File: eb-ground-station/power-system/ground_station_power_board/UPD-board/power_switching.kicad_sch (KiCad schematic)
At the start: 22 parts

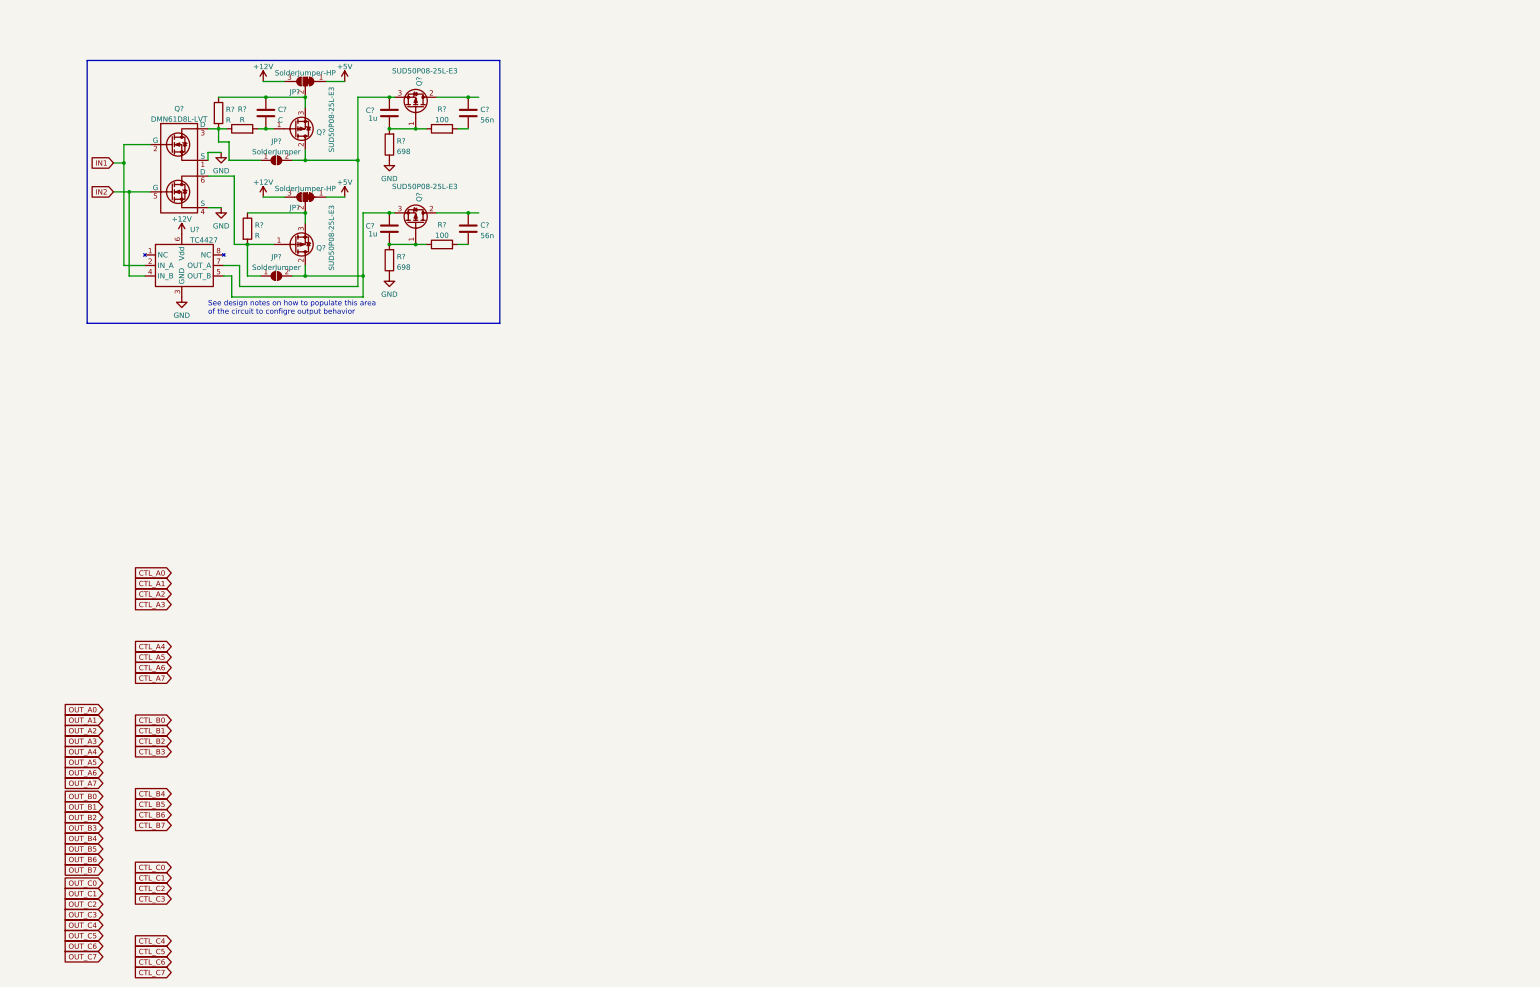
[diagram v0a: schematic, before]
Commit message: New power board schematic almost done
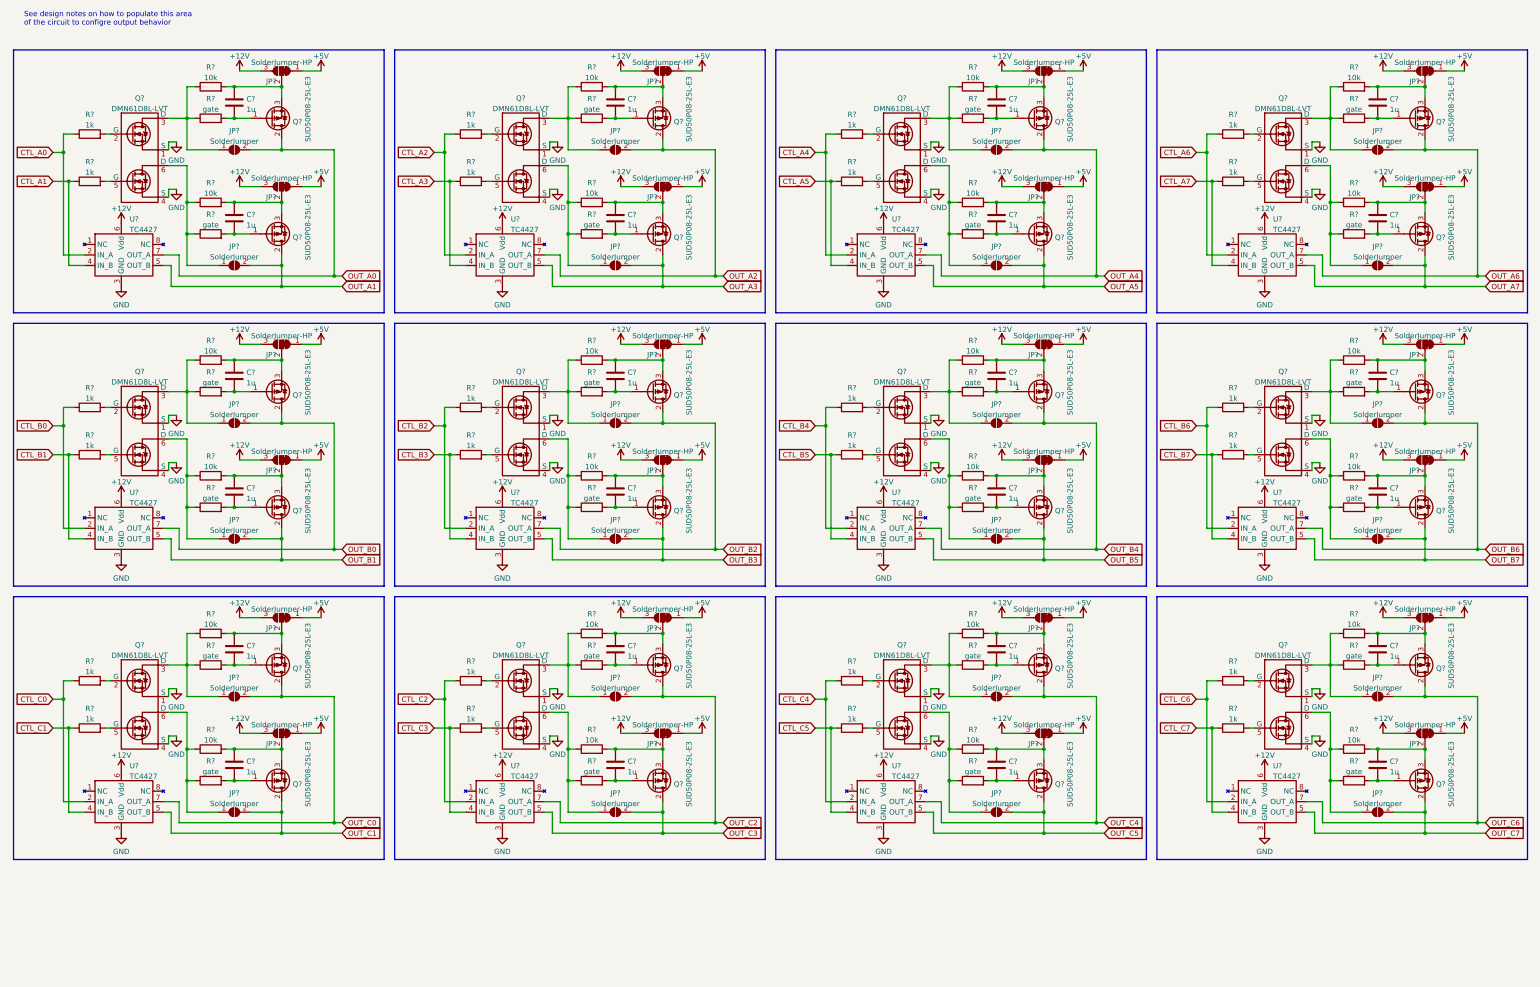
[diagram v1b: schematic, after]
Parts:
- removed C? (x2): 1u, symbol Device:C
- removed C? (x2): 56n, symbol Device:C
- removed Q? (x2): SUD50P08-25L-E3, symbol Device:Q_PMOS_GDS
- removed R? (x2): 698, symbol Device:R
- removed R? (x2): 100, symbol Device:R
- added C? (x23): 1u, symbol Device:C
- added JP? (x22): SolderJumper, symbol Jumper:SolderJumper_2_Open
- added JP? (x22): SolderJumper-HP, symbol Jumper:SolderJumper_3_Bridged12
- added Q? (x11): DMN61D8L-LVT, symbol OreSat-q-mosfet-DMN61D8L-LVT:DMN61D8L-LVT
- added Q? (x22): SUD50P08-25L-E3, symbol Device:Q_PMOS_GDS
- added R? (x24): 1k, symbol Device:R
- added R? (x23): gate, symbol Device:R
- added R? (x22): 10k, symbol Device:R
- added U? (x11): TC4427, symbol OreSat-q-mosfet-driver-TC4427:TC4427
- C?: value C -> 1u
- R? (x2): value R -> 10k
- R?: value R -> gate
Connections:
- net +12V: now also JP?.3 (B), JP?.3 (B), JP?.3 (B), JP?.3 (B), JP?.3 (B), JP?.3 (B), JP?.3 (B), JP?.3 (B), JP?.3 (B), JP?.3 (B), JP?.3 (B), JP?.3 (B), JP?.3 (B), JP?.3 (B), JP?.3 (B), JP?.3 (B), JP?.3 (B), JP?.3 (B), JP?.3 (B), JP?.3 (B), JP?.3 (B), JP?.3 (B), U?.6 (Vdd), U?.6 (Vdd), U?.6 (Vdd), U?.6 (Vdd), U?.6 (Vdd), U?.6 (Vdd), U?.6 (Vdd), U?.6 (Vdd), U?.6 (Vdd), U?.6 (Vdd), U?.6 (Vdd)
- net +5V: now also JP?.1 (A), JP?.1 (A), JP?.1 (A), JP?.1 (A), JP?.1 (A), JP?.1 (A), JP?.1 (A), JP?.1 (A), JP?.1 (A), JP?.1 (A), JP?.1 (A), JP?.1 (A), JP?.1 (A), JP?.1 (A), JP?.1 (A), JP?.1 (A), JP?.1 (A), JP?.1 (A), JP?.1 (A), JP?.1 (A), JP?.1 (A), JP?.1 (A)
- net CTL_A0: now also U?.2 (IN_A), R?.1
- net CTL_A1: now also U?.4 (IN_B), R?.1
- net CTL_A2: now also R?.1, U?.2 (IN_A)
- net CTL_A3: now also R?.1, U?.4 (IN_B)
- net CTL_A4: now also R?.1, U?.2 (IN_A)
- net CTL_A5: now also R?.1, U?.4 (IN_B)
- net CTL_A6: now also R?.1, U?.2 (IN_A)
- net CTL_A7: now also R?.1, U?.4 (IN_B)
- net CTL_B0: now also R?.1, U?.2 (IN_A)
- net CTL_B1: now also R?.1, U?.4 (IN_B)
- net CTL_B2: now also R?.1, U?.2 (IN_A)
- net CTL_B3: now also R?.1, U?.4 (IN_B)
- net CTL_B4: now also R?.1, U?.2 (IN_A)
- net CTL_B5: now also R?.1, U?.4 (IN_B)
- net CTL_B6: now also R?.1, U?.2 (IN_A)
- net CTL_B7: now also R?.1, U?.4 (IN_B)
- net CTL_C0: now also R?.1, U?.2 (IN_A)
- net CTL_C1: now also R?.1, U?.4 (IN_B)
- net CTL_C2: now also R?.1, U?.2 (IN_A)
- net CTL_C3: now also R?.1, U?.4 (IN_B)
- net CTL_C4: now also R?.1, U?.2 (IN_A)
- net CTL_C5: now also R?.1, U?.4 (IN_B)
- net CTL_C6: now also R?.1, U?.2 (IN_A)
- net CTL_C7: now also R?.1, U?.4 (IN_B)
- net GND: now also Q?.1 (S), Q?.1 (S), Q?.1 (S), Q?.1 (S), Q?.1 (S), Q?.1 (S), Q?.1 (S), Q?.1 (S), Q?.1 (S), Q?.1 (S), Q?.1 (S), Q?.4 (S), Q?.4 (S), Q?.4 (S), Q?.4 (S), Q?.4 (S), Q?.4 (S), Q?.4 (S), Q?.4 (S), Q?.4 (S), Q?.4 (S), Q?.4 (S), U?.3 (GND), U?.3 (GND), U?.3 (GND), U?.3 (GND), U?.3 (GND), U?.3 (GND), U?.3 (GND), U?.3 (GND), U?.3 (GND), U?.3 (GND), U?.3 (GND)
- net OUT_A0: now also JP?.2 (B), Q?.2 (D), U?.7 (OUT_A)
- net OUT_A1: now also JP?.2 (B), Q?.2 (D), U?.5 (OUT_B)
- net OUT_A2: now also JP?.2 (B), Q?.2 (D), U?.7 (OUT_A)
- net OUT_A3: now also JP?.2 (B), Q?.2 (D), U?.5 (OUT_B)
- net OUT_A4: now also JP?.2 (B), Q?.2 (D), U?.7 (OUT_A)
- net OUT_A5: now also JP?.2 (B), Q?.2 (D), U?.5 (OUT_B)
- net OUT_A6: now also JP?.2 (B), Q?.2 (D), U?.7 (OUT_A)
- net OUT_A7: now also JP?.2 (B), Q?.2 (D), U?.5 (OUT_B)
- net OUT_B0: now also JP?.2 (B), Q?.2 (D), U?.7 (OUT_A)
- net OUT_B1: now also JP?.2 (B), Q?.2 (D), U?.5 (OUT_B)
- net OUT_B2: now also JP?.2 (B), Q?.2 (D), U?.7 (OUT_A)
- net OUT_B3: now also JP?.2 (B), Q?.2 (D), U?.5 (OUT_B)
- net OUT_B4: now also JP?.2 (B), Q?.2 (D), U?.7 (OUT_A)
- net OUT_B5: now also JP?.2 (B), Q?.2 (D), U?.5 (OUT_B)
- net OUT_B6: now also JP?.2 (B), Q?.2 (D), U?.7 (OUT_A)
- net OUT_B7: now also JP?.2 (B), Q?.2 (D), U?.5 (OUT_B)
- net OUT_C0: now also JP?.2 (B), Q?.2 (D), U?.7 (OUT_A)
- net OUT_C1: now also JP?.2 (B), Q?.2 (D), U?.5 (OUT_B)
- net OUT_C2: now also JP?.2 (B), Q?.2 (D), U?.7 (OUT_A)
- net OUT_C3: now also JP?.2 (B), Q?.2 (D), U?.5 (OUT_B)
- net OUT_C4: now also JP?.2 (B), Q?.2 (D), U?.7 (OUT_A)
- net OUT_C5: now also JP?.2 (B), Q?.2 (D), U?.5 (OUT_B)
- net OUT_C6: now also JP?.2 (B), Q?.2 (D), U?.7 (OUT_A)
- net OUT_C7: now also JP?.2 (B), Q?.2 (D), U?.5 (OUT_B)
- net at C?.1, JP?.2 (C), Q?.3 (S): now also R?.2; no longer R?.1
- net at JP?.1 (A), Q?.3 (D), R?.1: now also R?.1; no longer R?.2
- net at JP?.2 (C), Q?.3 (S): now also R?.2, C?.1; no longer R?.1
- net at JP?.1 (A), Q?.6 (D): now also R?.1, R?.1; no longer Q?.1 (G), R?.2
- net IN1: no longer names the net of Q?.2 (G)
- net IN1: now also R?.2; no longer U?.2 (IN_A)
- net IN2: no longer names the net of Q?.5 (G)
- net IN2: now also R?.2; no longer U?.4 (IN_B)
- new net: Q?.2 (G), R?.2 (x11)
- new net: JP?.1 (A), Q?.3 (D), R?.1, R?.1 (x11)
- new net: Q?.5 (G), R?.2 (x11)
- new net: JP?.1 (A), Q?.6 (D), R?.1, R?.1 (x11)
- new net: C?.2, Q?.1 (G), R?.2 (x23)
- new net: C?.1, JP?.2 (C), Q?.3 (S), R?.2 (x22)
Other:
- moved on the sheet: C?, JP?, Q?, R?, U?

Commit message: First layout done. No slikscreen work yet
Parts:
- removed C? (x16): 1u, symbol Device:C
- removed JP? (x16): SolderJumper, symbol Jumper:SolderJumper_2_Open
- removed JP? (x20): SolderJumper-HP, symbol Jumper:SolderJumper_3_Bridged12
- removed Q? (x7): DMN61D8L-LVT, symbol OreSat-q-mosfet-DMN61D8L-LVT:DMN61D8L-LVT
- removed Q? (x16): SUD50P08-25L-E3, symbol Device:Q_PMOS_GDS
- removed R? (x24): 1k, symbol Device:R
- removed R? (x16): gate, symbol Device:R
- removed R? (x16): 10k, symbol Device:R
- removed U? (x7): TC4427, symbol OreSat-q-mosfet-driver-TC4427:TC4427
- added Q10, Q13, Q14, Q2, Q6, Q7, Q9: DMN61D8L-LVT, oresat-footprints:TSOT26-6, symbol OreSat-q-mosfet-DMN61D8L-LVT:DMN61D8L-LVT
- added RN13, RN14, RN15, RN16, RN17, RN18: 10k, Resistor_SMD:R_Array_Convex_4x0603, symbol Device:R_Pack04
- added U10, U11, U12, U14, U15, U16, U17: TC4427, Package_SO:MSOP-8_3x3mm_P0.65mm, symbol OreSat-q-mosfet-driver-TC4427:TC4427
- C12, C13, C14, C15, C16, C17, C18, C19: renamed from C?; footprint (none) -> Capacitor_SMD:C_0603_1608Metric; DPN (none) -> 1276-1184-2-ND; MPN (none) -> CL10B105KA8NNNC; Mfr (none) -> Samsung Electro-Mechanics
- JP14, JP15, JP18, JP19, JP22, JP23, JP26, JP27: renamed from JP?; footprint (none) -> oresat-footprints:SolderJumper-2_P1.3mm_Open_RoundedPad1.0x1.5mm
- JP24, JP25, JP28, JP29: renamed from JP?; footprint (none) -> oresat-footprints:JP-SOLDER-2way-HP
- Q1, Q15, Q18, Q3, Q8: renamed from Q?; footprint (none) -> oresat-footprints:TSOT26-6
- Q11, Q12, Q16, Q17, Q19, Q20, Q4, Q5: renamed from Q?; footprint (none) -> oresat-footprints:TO-252-3_TabIsPin2
- R10, R11, R12, R13, R14, R15, R16, R17, R18, R19, R20, R21, R22, R23, R8, R9: renamed from R?; footprint (none) -> Resistor_SMD:R_0603_1608Metric
- U13, U18, U19, U8, U9: renamed from U?; footprint (none) -> Package_SO:MSOP-8_3x3mm_P0.65mm
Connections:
- net +12V: now also C14.1, C15.1, Q11.3 (S), Q12.3 (S), R12.2, R14.2, U10.6 (Vdd), U11.6 (Vdd), U12.6 (Vdd), U14.6 (Vdd), U15.6 (Vdd), U16.6 (Vdd), U17.6 (Vdd)
- net +5V: now also C12.1, C13.1, Q4.3 (S), Q5.3 (S), R10.2, R8.2
- net CTL_A0: now also RN13.5 (R4.2)
- net CTL_A1: now also RN13.6 (R3.2)
- net CTL_A2: now also RN13.7 (R2.2)
- net CTL_A3: now also RN13.8 (R1.2)
- net CTL_A4: now also RN14.4 (R4.1)
- net CTL_A5: now also RN14.3 (R3.1)
- net CTL_A6: now also RN14.2 (R2.1)
- net CTL_A7: now also RN14.1 (R1.1)
- net CTL_B0: now also RN15.4 (R4.1)
- net CTL_B1: now also RN15.3 (R3.1)
- net CTL_B2: now also RN15.2 (R2.1), U11.2 (IN_A)
- net CTL_B3: now also RN15.1 (R1.1), U11.4 (IN_B)
- net CTL_B4: now also RN16.4 (R4.1), U14.2 (IN_A)
- net CTL_B5: now also RN16.3 (R3.1), U14.4 (IN_B)
- net CTL_B6: now also RN16.2 (R2.1), U16.2 (IN_A)
- net CTL_B7: now also RN16.1 (R1.1), U16.4 (IN_B)
- net CTL_C0: now also RN17.4 (R4.1), U10.2 (IN_A)
- net CTL_C1: now also RN17.3 (R3.1), U10.4 (IN_B)
- net CTL_C2: now also RN17.2 (R2.1), U12.2 (IN_A)
- net CTL_C3: now also RN17.1 (R1.1), U12.4 (IN_B)
- net CTL_C4: now also RN18.4 (R4.1), U15.2 (IN_A)
- net CTL_C5: now also RN18.3 (R3.1), U15.4 (IN_B)
- net CTL_C6: now also RN18.2 (R2.1), U17.2 (IN_A)
- net CTL_C7: now also RN18.1 (R1.1), U17.4 (IN_B)
- net GND: now also Q10.1 (S), Q10.4 (S), Q13.1 (S), Q13.4 (S), Q14.1 (S), Q14.4 (S), Q2.1 (S), Q2.4 (S), Q6.1 (S), Q6.4 (S), Q7.1 (S), Q7.4 (S), Q9.1 (S), Q9.4 (S), U10.3 (GND), U11.3 (GND), U12.3 (GND), U14.3 (GND), U15.3 (GND), U16.3 (GND), U17.3 (GND)
- net OUT_B0: now also Q1.3 (D)
- net OUT_B1: now also Q1.6 (D)
- net OUT_B2: now also Q6.3 (D), U11.7 (OUT_A)
- net OUT_B3: now also Q6.6 (D), U11.5 (OUT_B)
- net OUT_B4: now also Q9.3 (D), U14.7 (OUT_A)
- net OUT_B5: now also Q9.6 (D), U14.5 (OUT_B)
- net OUT_B6: now also Q13.3 (D), U16.7 (OUT_A)
- net OUT_B7: now also Q13.6 (D), U16.5 (OUT_B)
- net OUT_C0: now also Q2.3 (D), U10.7 (OUT_A)
- net OUT_C1: now also Q2.6 (D), U10.5 (OUT_B)
- net OUT_C2: now also Q7.3 (D), U12.7 (OUT_A)
- net OUT_C3: now also Q7.6 (D), U12.5 (OUT_B)
- net OUT_C4: now also Q10.3 (D), U15.7 (OUT_A)
- net OUT_C5: now also Q10.6 (D), U15.5 (OUT_B)
- net OUT_C6: now also Q14.3 (D), U17.7 (OUT_A)
- net OUT_C7: now also Q14.6 (D), U17.5 (OUT_B)
- net MOS_A4: now reaches Q15.2 (G)
- net MOS_A4: now also RN14.5 (R4.2)
- net MOS_B0: now reaches Q1.2 (G)
- net MOS_B0: now also RN15.5 (R4.2)
- net MOS_B1: now reaches Q1.5 (G)
- net MOS_B1: now also RN15.6 (R3.2)
- net MOS_A5: now reaches Q15.5 (G)
- net MOS_A5: now also RN14.6 (R3.2)
- net MOS_A0: now reaches Q3.2 (G)
- net MOS_A0: now also RN13.4 (R4.1)
- net MOS_A6: now reaches Q18.2 (G)
- net MOS_A6: now also RN14.7 (R2.2)
- net MOS_A2: now reaches Q8.2 (G)
- net MOS_A2: now also RN13.2 (R2.1)
- net MOS_A7: now reaches Q18.5 (G)
- net MOS_A7: now also RN14.8 (R1.2)
- net MOS_A1: now reaches Q3.5 (G)
- net MOS_A1: now also RN13.3 (R3.1)
- net MOS_A3: now reaches Q8.5 (G)
- net MOS_A3: now also RN13.1 (R1.1)
- new net MOS_B2: Q6.2 (G), RN15.7 (R2.2)
- new net MOS_B3: Q6.5 (G), RN15.8 (R1.2)
- new net MOS_B4: Q9.2 (G), RN16.5 (R4.2)
- new net MOS_B5: Q9.5 (G), RN16.6 (R3.2)
- new net MOS_B6: Q13.2 (G), RN16.7 (R2.2)
- new net MOS_B7: Q13.5 (G), RN16.8 (R1.2)
- new net MOS_C0: Q2.2 (G), RN17.5 (R4.2)
- new net MOS_C1: Q2.5 (G), RN17.6 (R3.2)
- new net MOS_C2: Q7.2 (G), RN17.7 (R2.2)
- new net MOS_C3: Q7.5 (G), RN17.8 (R1.2)
- new net MOS_C4: Q10.2 (G), RN18.5 (R4.2)
- new net MOS_C5: Q10.5 (G), RN18.6 (R3.2)
- new net MOS_C6: Q14.2 (G), RN18.7 (R2.2)
- new net MOS_C7: Q14.5 (G), RN18.8 (R1.2)
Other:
- note added: "All channels can do the -500mA and ±1.5A ranges."
- note added: "Bank A"
- note added: "Bank B"
- note added: "Bank C"
- note added: "Channel Configuration Instructions:"
- note added: "Each channel or pair has several configurable output modes."
- note added: "For Bank A:"
- note added: "For Banks B and C:"
- note added: "For the +10A range:"
- note added: "For the -500mA and +10A ranges:"
- note added: "For the -500mA range: Jump the 2 position jumper for that channel"
- note added: "For the -500mA range: Populate the dual MOSFET only"
- note added: "For the ±1.5A range: Populate the dual MOSFET driver only"
- note added: "Gate Resistors"
- note added: "Jump the 3 position jumper to select the voltage"
- note added: "Never populate the dual MOSFET and the MOSFET driver on the same channel pair"
- note added: "Only channel A can do the +10A with optional soft start range."
- note added: "Populate the P-FET, the 10K resistor, and a 1k gate resistor"
- note added: "Populate the dual MOSFET"
- note added: "Ranges: -500mA ±1.5A"
- note added: "Ranges: -500mA ±1.5A +10A"
- note added: "The two channels in the pair may be configured independently"
- note added: "To add soft start: Use a 680k gate resistor and populate the capacitor"
- moved on the sheet: C12, C13, C14, C15, C16, C17, C18, C19, JP14, JP15, JP18, JP19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

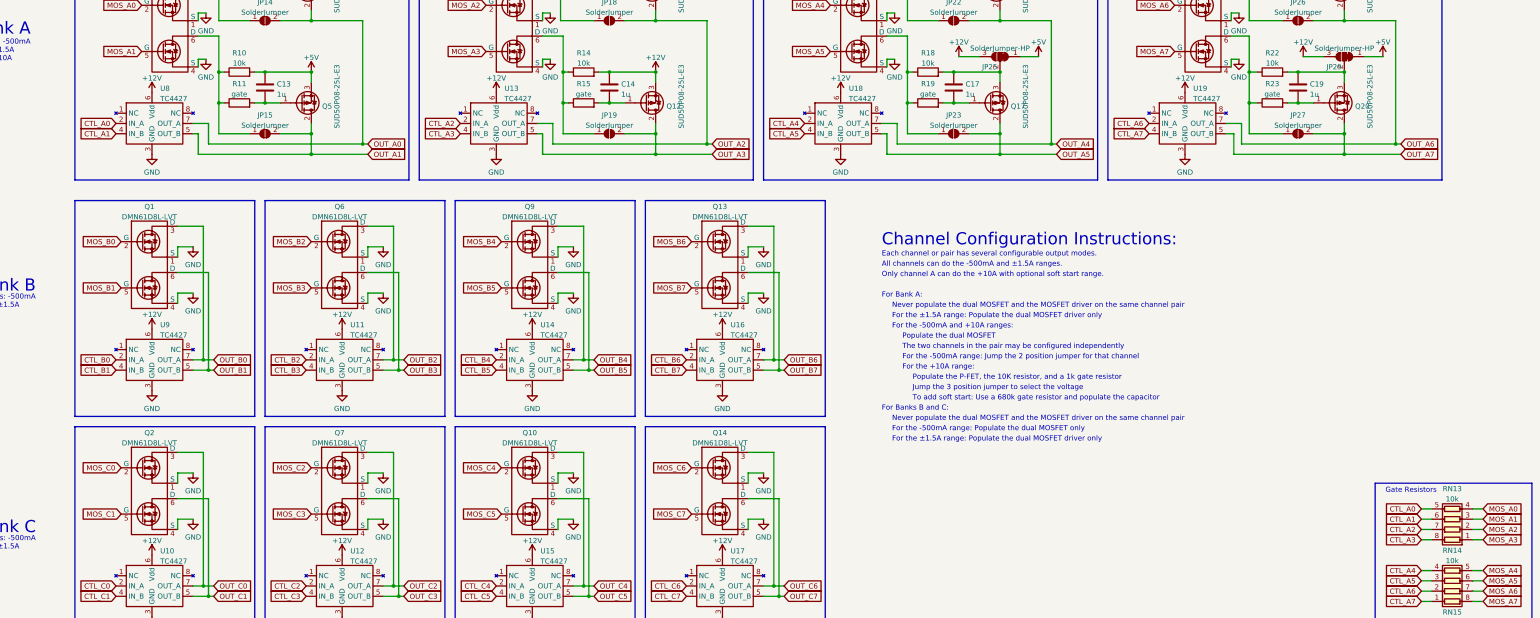
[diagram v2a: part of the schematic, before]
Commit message: Upgrading Bank A to 16A
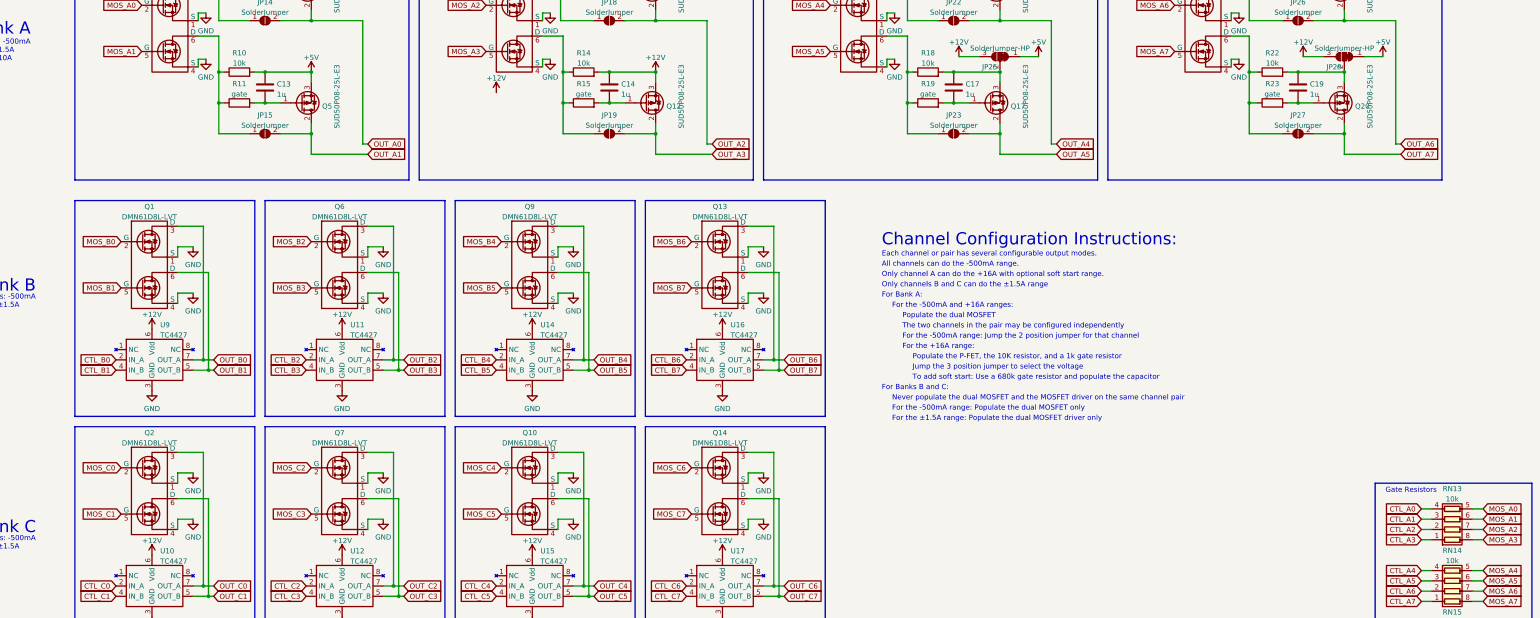
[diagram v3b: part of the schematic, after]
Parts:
- removed U13, U18, U19, U8: TC4427, Package_SO:MSOP-8_3x3mm_P0.65mm, symbol OreSat-q-mosfet-driver-TC4427:TC4427
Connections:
- net CTL_A0: now also RN13.4 (R4.1); no longer RN13.5 (R4.2)
- net CTL_A1: now also RN13.3 (R3.1); no longer RN13.6 (R3.2)
- net CTL_A2: now also RN13.2 (R2.1); no longer RN13.7 (R2.2)
- net CTL_A3: now also RN13.1 (R1.1); no longer RN13.8 (R1.2)
- net MOS_A0: now also RN13.5 (R4.2); no longer RN13.4 (R4.1)
- net MOS_A1: now also RN13.6 (R3.2); no longer RN13.3 (R3.1)
- net MOS_A2: now also RN13.7 (R2.2); no longer RN13.2 (R2.1)
- net MOS_A3: now also RN13.8 (R1.2); no longer RN13.1 (R1.1)
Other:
- note added: "All channels can do the -500mA range."
- note added: "For the +16A range:"
- note added: "For the -500mA and +16A ranges:"
- note added: "Only channel A can do the +16A with optional soft start range."
- note added: "Only channels B and C can do the ±1.5A range"
- note removed: "All channels can do the -500mA and ±1.5A ranges."
- note removed: "For the +10A range:"
- note removed: "For the -500mA and +10A ranges:"
- note removed: "Only channel A can do the +10A with optional soft start range."
- moved on the sheet: RN13
